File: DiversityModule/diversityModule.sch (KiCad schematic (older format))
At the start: 41 parts, among them IC1 LP38798, IC2 TDA1308A, P1 CONN_02X05, P2 CONN_01X03, Q1 BFP840, U1 sn74lvc1g3157, U2 RX5808

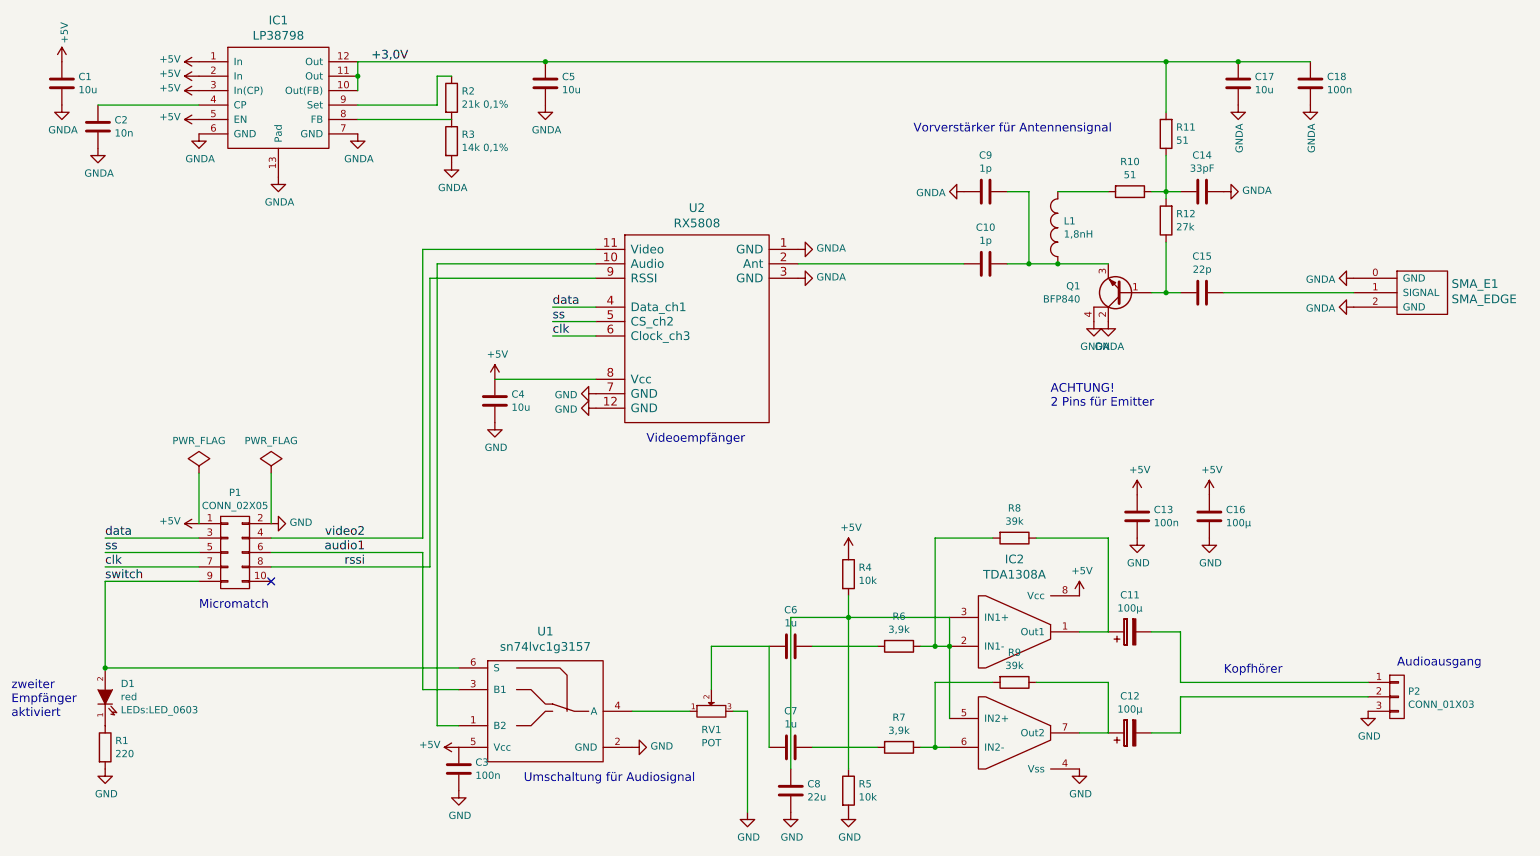
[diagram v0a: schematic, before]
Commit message: Layout fertig. Überprüfung steht aus.
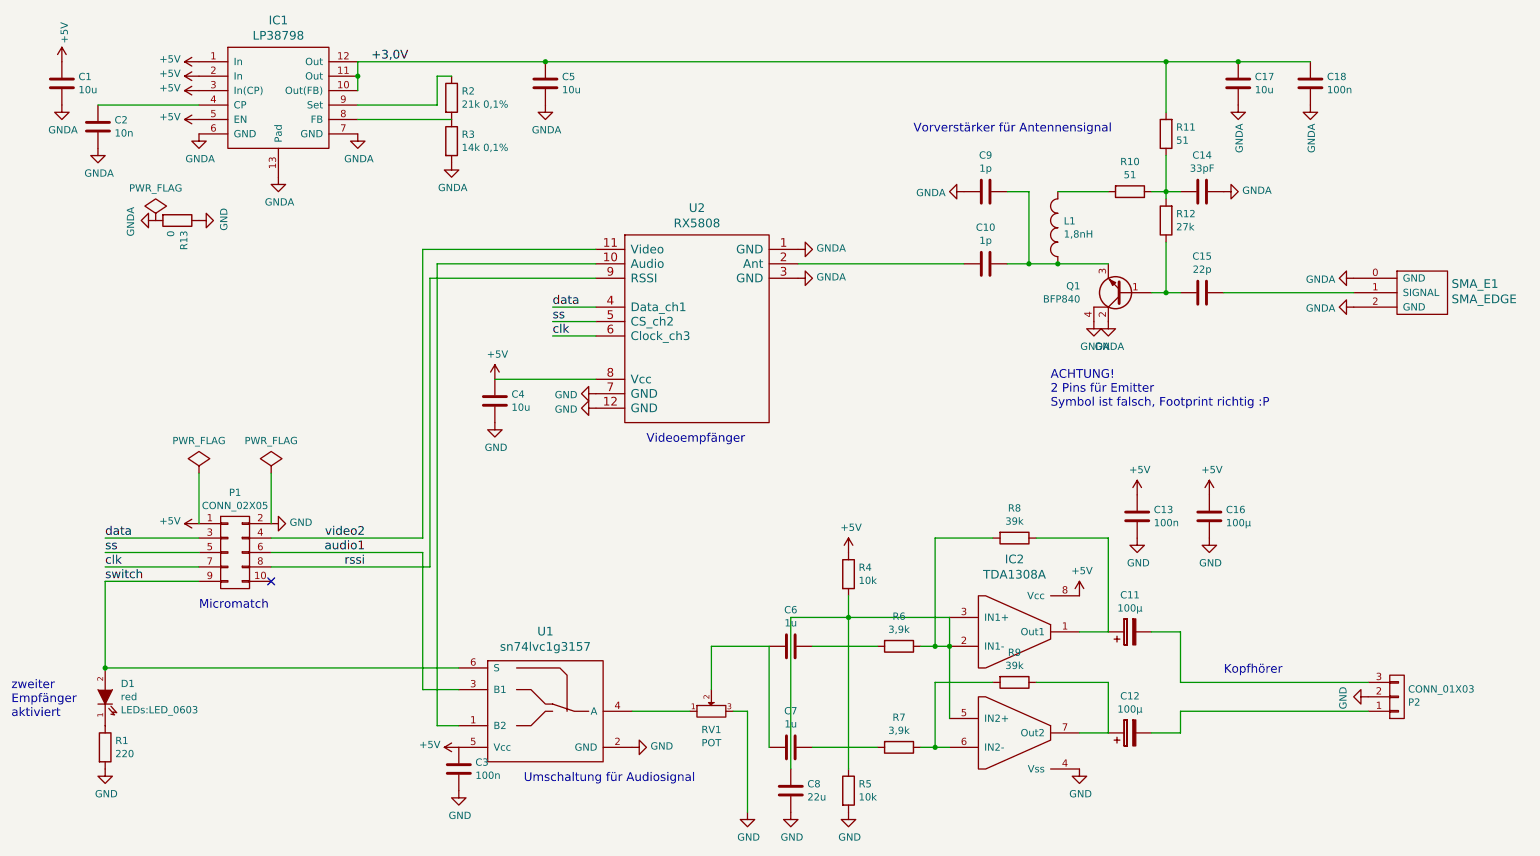
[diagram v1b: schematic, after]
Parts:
- added R13: 0, Resistors_SMD:R_0805, symbol R
- P2: footprint (none) -> PhilippsFootprints:LUM1503-SMD
- RV1: footprint (none) -> PhilippsFootprints:Poti-SMD-Model-23A
- U1: footprint TO_SOT_Packages_SMD:SOT-23-5 -> TO_SOT_Packages_SMD:SOT-23-6
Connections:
- net GND: now also P2.2 (P2), R13.1; no longer P2.3 (P3)
- net GNDA: now also R13.2
- net at P2.1 (P1): now also C12.2; no longer C11.2
- new net: C11.2, P2.3 (P3)
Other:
- note added: "ACHTUNG!\n2 Pins für Emitter\nSymbol ist falsch, Footprint richtig :P"
- note removed: "ACHTUNG!\n2 Pins für Emitter"
- note removed: "Audioausgang"
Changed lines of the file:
@@
 F 0 "U1" H 4400 6053 60  0000 C CNN
 F 1 "sn74lvc1g3157" H 4400 5947 60  0000 C CNN
-F 2 "TO_SOT_Packages_SMD:SOT-23-5" H 3150 5000 60  0001 C CNN
+F 2 "TO_SOT_Packages_SMD:SOT-23-6" H 3150 5000 60  0001 C CNN
 F 3 "" H 3150 5000 60  0000 C CNN
 	1    4400 5500
@@
 F 0 "P2" H 10377 5438 50  0000 L CNN
 F 1 "CONN_01X03" H 10377 5347 50  0000 L CNN
-F 2 "" H 10300 5400 50  0001 C CNN
+F 2 "PhilippsFootprints:LUM1503-SMD" H 10300 5400 50  0001 C CNN
 F 3 "" H 10300 5400 50  0000 C CNN
 	1    10300 5400
-	1    0    0    -1
+	1    0    0    1
 $EndComp
 $Comp
 L GND #PWR013
 U 1 1 5706CAFE
-P 10100 5500
-F 0 "#PWR013" H 10100 5250 50  0001 C CNN
-F 1 "GND" H 10108 5327 50  0000 C CNN
-F 2 "" H 10100 5500 50  0000 C CNN
-F 3 "" H 10100 5500 50  0000 C CNN
-	1    10100 5500
-	1    0    0    -1
+P 10100 5400
+F 0 "#PWR013" H 10100 5150 50  0001 C CNN
+F 1 "GND" H 10108 5227 50  0000 C CNN
+F 2 "" H 10100 5400 50  0000 C CNN
+F 3 "" H 10100 5400 50  0000 C CNN
+	1    10100 5400
+	0    1    1    0
 $EndComp
 Connection ~ 1350 5200
@@
 Text Notes 5100 3650 0    60   ~ 0
 Videoempfänger
-Text Notes 10300 5200 0    60   ~ 0
-Audioausgang
 Text Notes 700  5550 0    60   ~ 0
 zweiter\nEmpfänger\naktiviert
@@
 F 0 "RV1" H 5550 5372 50  0000 C CNN
 F 1 "POT" H 5550 5281 50  0000 C CNN
-F 2 "" H 5550 5500 50  0001 C CNN
+F 2 "PhilippsFootprints:Poti-SMD-Model-23A" H 5550 5500 50  0001 C CNN
 F 3 "" H 5550 5500 50  0000 C CNN
 	1    5550 5500
@@
 Wire Wire Line
 	8600 5650 8800 5650
-Wire Wire Line
-	8800 5650 8800 5400
-Wire Wire Line
-	8800 5400 10100 5400
 Wire Wire Line
 	8600 4950 8800 4950
@@
 $EndComp
 Text Notes 7900 3400 0    60   ~ 0
-ACHTUNG!\n2 Pins für Emitter
+ACHTUNG!\n2 Pins für Emitter\nSymbol ist falsch, Footprint richtig :P
 $Comp
 L GNDA #PWR024
@@
 Connection ~ 8700 1000
 Connection ~ 9200 1000
+Wire Wire Line
+	10100 5500 8800 5500
+Wire Wire Line
+	8800 5500 8800 5650
+$Comp
+L R R13
+U 1 1 570E7730
+P 1850 2100
+F 0 "R13" H 1920 2146 50  0000 L CNN
+F 1 "0" H 1920 2055 50  0000 L CNN
+F 2 "Resistors_SMD:R_0805" V 1780 2100 50  0001 C CNN
+F 3 "" H 1850 2100 50  0000 C CNN
+F 4 "YAG1783CT-ND" H 1850 2100 60  0001 C CNN "Digikeynummer"
+	1    1850 2100
+	0    1    1    0
+$EndComp
+$Comp
+L GNDA #PWR046
+U 1 1 570E786B
+P 1700 2100
+F 0 "#PWR046" H 1700 1850 50  0001 C CNN
+F 1 "GNDA" H 1708 1927 50  0000 C CNN
+F 2 "" H 1700 2100 50  0000 C CNN
+F 3 "" H 1700 2100 50  0000 C CNN
+	1    1700 2100
+	0    1    1    0
+$EndComp
+$Comp
+L GND #PWR047
+U 1 1 570E7948
+P 2000 2100
+F 0 "#PWR047" H 2000 1850 50  0001 C CNN
+F 1 "GND" H 2008 1927 50  0000 C CNN
+F 2 "" H 2000 2100 50  0000 C CNN
+F 3 "" H 2000 2100 50  0000 C CNN
+	1    2000 2100
+	0    -1   -1   0
+$EndComp
+$Comp
+L PWR_FLAG #FLG048
+U 1 1 570E7D78
+P 1700 2100
+F 0 "#FLG048" H 1700 2195 50  0001 C CNN
+F 1 "PWR_FLAG" H 1700 2324 50  0000 C CNN
+F 2 "" H 1700 2100 50  0000 C CNN
+F 3 "" H 1700 2100 50  0000 C CNN
+	1    1700 2100
+	1    0    0    -1
+$EndComp
 $EndSCHEMATC

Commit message: BOM für beide platinen des kompletten moduls dazugefügt
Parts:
- SMA_E1: footprint PhilippsFootprints:SMA_EDGE_small -> PhilippsFootprints:SMA_EDGE_Johnson_142-0701-801
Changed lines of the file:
@@
 F 0 "SMA_E1" H 10678 2661 60  0000 L CNN
 F 1 "SMA_EDGE" H 10678 2555 60  0000 L CNN
-F 2 "PhilippsFootprints:SMA_EDGE_small" H 10350 2600 60  0001 C CNN
+F 2 "PhilippsFootprints:SMA_EDGE_Johnson_142-0701-801" H 10350 2600 60  0001 C CNN
 F 3 "" H 10350 2600 60  0000 C CNN
 	1    10350 2600

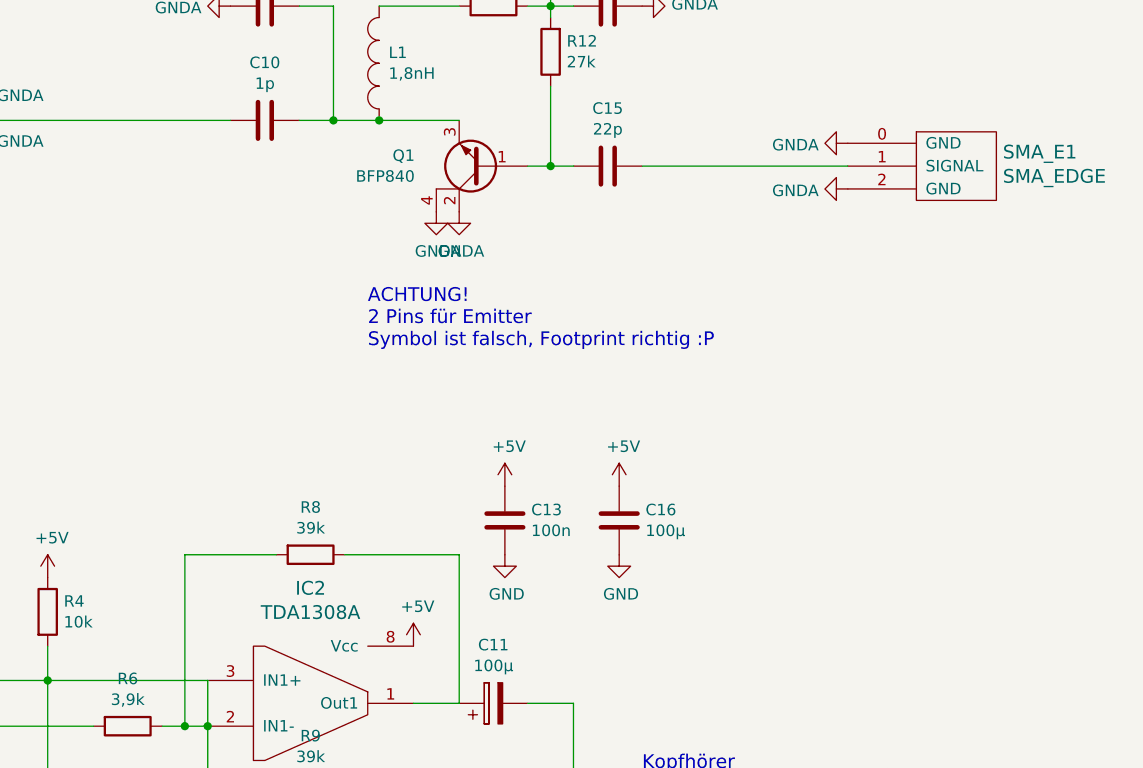
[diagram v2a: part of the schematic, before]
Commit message: Layoutänderungen für videoumschalter (anderes gehäuse)
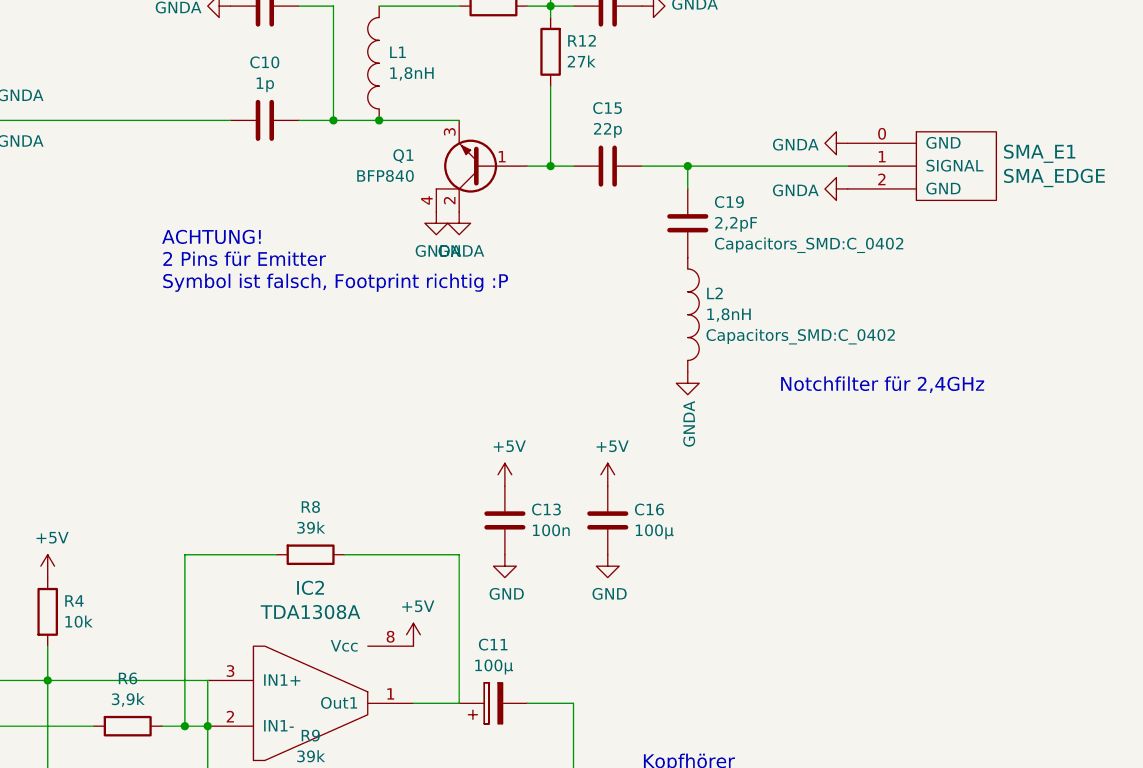
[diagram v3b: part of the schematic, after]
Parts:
- added C19: 2,2pF, Capacitors_SMD:C_0402, symbol C
- added L2: 1,8nH, Capacitors_SMD:C_0402, symbol INDUCTOR_SMALL
- U1: footprint TO_SOT_Packages_SMD:SOT-23-6 -> TO_SOT_Packages_SMD:SC-70-6
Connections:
- net GNDA: now also L2.2
- net at C15.1, SMA_E1.1 (SIGNAL): now also C19.1
- new net: C19.2, L2.1
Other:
- note added: "Notchfilter für 2,4GHz"
- moved on the sheet: C16
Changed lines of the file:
@@
 Title "Diversity-Zusatzmodul"
 Date "2016-04-07"
-Rev "0.1"
+Rev "0.2"
 Comp ""
 Comment1 ""
@@
 F 0 "U1" H 4400 6053 60  0000 C CNN
 F 1 "sn74lvc1g3157" H 4400 5947 60  0000 C CNN
-F 2 "TO_SOT_Packages_SMD:SOT-23-6" H 3150 5000 60  0001 C CNN
+F 2 "TO_SOT_Packages_SMD:SC-70-6" H 3150 5000 60  0001 C CNN
 F 3 "" H 3150 5000 60  0000 C CNN
 	1    4400 5500
@@
 L C C16
 U 1 1 5706F496
-P 9000 4150
-F 0 "C16" H 9115 4196 50  0000 L CNN
-F 1 "100µ" H 9115 4105 50  0000 L CNN
-F 2 "Capacitors_SMD:C_1210" H 9038 4000 50  0001 C CNN
-F 3 "" H 9000 4150 50  0000 C CNN
-	1    9000 4150
+P 8950 4150
+F 0 "C16" H 9065 4196 50  0000 L CNN
+F 1 "100µ" H 9065 4105 50  0000 L CNN
+F 2 "Capacitors_SMD:C_1210" H 8988 4000 50  0001 C CNN
+F 3 "" H 8950 4150 50  0000 C CNN
+	1    8950 4150
 	1    0    0    -1
 $EndComp
@@
 L GND #PWR021
 U 1 1 5706F561
-P 9000 4300
-F 0 "#PWR021" H 9000 4050 50  0001 C CNN
-F 1 "GND" H 9008 4127 50  0000 C CNN
-F 2 "" H 9000 4300 50  0000 C CNN
-F 3 "" H 9000 4300 50  0000 C CNN
-	1    9000 4300
+P 8950 4300
+F 0 "#PWR021" H 8950 4050 50  0001 C CNN
+F 1 "GND" H 8958 4127 50  0000 C CNN
+F 2 "" H 8950 4300 50  0000 C CNN
+F 3 "" H 8950 4300 50  0000 C CNN
+	1    8950 4300
 	1    0    0    -1
 $EndComp
@@
 L +5V #PWR023
 U 1 1 5706F6CB
-P 9000 4000
-F 0 "#PWR023" H 9000 3850 50  0001 C CNN
-F 1 "+5V" H 9018 4173 50  0000 C CNN
-F 2 "" H 9000 4000 50  0000 C CNN
-F 3 "" H 9000 4000 50  0000 C CNN
-	1    9000 4000
+P 8950 4000
+F 0 "#PWR023" H 8950 3850 50  0001 C CNN
+F 1 "+5V" H 8968 4173 50  0000 C CNN
+F 2 "" H 8950 4000 50  0000 C CNN
+F 3 "" H 8950 4000 50  0000 C CNN
+	1    8950 4000
 	1    0    0    -1
 $EndComp
@@
 	-1   0    0    1
 $EndComp
-Text Notes 7900 3400 0    60   ~ 0
+Text Notes 7000 3150 0    60   ~ 0
 ACHTUNG!\n2 Pins für Emitter\nSymbol ist falsch, Footprint richtig :P
 $Comp
@@
 	8700 2250 8700 2600
 Connection ~ 8700 2600
-Wire Wire Line
-	9100 2600 10000 2600
 $Comp
 L LP38798 IC1
@@
 	1    0    0    -1
 $EndComp
+$Comp
+L INDUCTOR_SMALL L2
+U 1 1 5756C8B7
+P 9300 3250
+F 0 "L2" V 9209 3328 50  0000 L CNN
+F 1 "1,8nH" V 9300 3328 50  0000 L CNN
+F 2 "Capacitors_SMD:C_0402" V 9391 3328 50  0000 L CNN
+F 3 "" H 9300 3250 50  0000 C CNN
+	1    9300 3250
+	0    1    1    0
+$EndComp
+$Comp
+L C C19
+U 1 1 5756CADB
+P 9300 2850
+F 0 "C19" H 9415 2941 50  0000 L CNN
+F 1 "2,2pF" H 9415 2850 50  0000 L CNN
+F 2 "Capacitors_SMD:C_0402" H 9415 2759 50  0000 L CNN
+F 3 "" H 9300 2850 50  0000 C CNN
+	1    9300 2850
+	1    0    0    -1
+$EndComp
+$Comp
+L GNDA #PWR049
+U 1 1 5756CC4F
+P 9300 3500
+F 0 "#PWR049" H 9300 3250 50  0001 C CNN
+F 1 "GNDA" V 9308 3373 50  0000 R CNN
+F 2 "" H 9300 3500 50  0000 C CNN
+F 3 "" H 9300 3500 50  0000 C CNN
+	1    9300 3500
+	1    0    0    -1
+$EndComp
+Wire Wire Line
+	10000 2600 9100 2600
+Wire Wire Line
+	9300 2700 9300 2600
+Connection ~ 9300 2600
+Text Notes 9700 3600 0    60   ~ 0
+Notchfilter für 2,4GHz
 $EndSCHEMATC

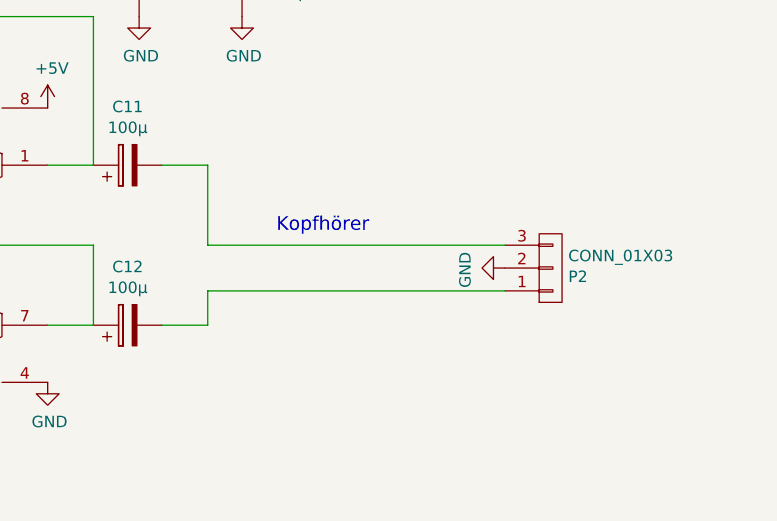
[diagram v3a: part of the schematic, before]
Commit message: Klinkenbuchse ausgetauscht und zur Lib hinzugefügt.
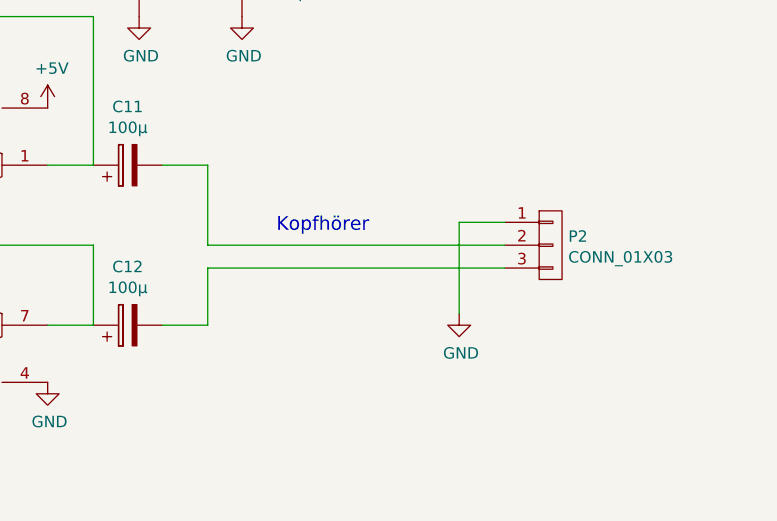
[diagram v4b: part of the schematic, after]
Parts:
- P2: footprint PhilippsFootprints:LUM1503-SMD -> PhilippsFootprints:LUM1503-03
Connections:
- net GND: now also P2.1 (P1); no longer P2.2 (P2)
- net at C12.2: now also P2.3 (P3); no longer P2.1 (P1)
- net at C11.2: now also P2.2 (P2); no longer P2.3 (P3)
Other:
- moved on the sheet: P2
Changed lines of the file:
@@
 L CONN_01X03 P2
 U 1 1 5706C9D5
-P 10300 5400
-F 0 "P2" H 10377 5438 50  0000 L CNN
-F 1 "CONN_01X03" H 10377 5347 50  0000 L CNN
-F 2 "PhilippsFootprints:LUM1503-SMD" H 10300 5400 50  0001 C CNN
-F 3 "" H 10300 5400 50  0000 C CNN
-	1    10300 5400
-	1    0    0    1
+P 10300 5300
+F 0 "P2" H 10377 5338 50  0000 L CNN
+F 1 "CONN_01X03" H 10377 5247 50  0000 L CNN
+F 2 "PhilippsFootprints:LUM1503-03" H 10300 5300 50  0001 C CNN
+F 3 "" H 10300 5300 50  0000 C CNN
+	1    10300 5300
+	1    0    0    -1
 $EndComp
 $Comp
 L GND #PWR013
 U 1 1 5706CAFE
-P 10100 5400
-F 0 "#PWR013" H 10100 5150 50  0001 C CNN
-F 1 "GND" H 10108 5227 50  0000 C CNN
-F 2 "" H 10100 5400 50  0000 C CNN
-F 3 "" H 10100 5400 50  0000 C CNN
-	1    10100 5400
-	0    1    1    0
+P 9900 5600
+F 0 "#PWR013" H 9900 5350 50  0001 C CNN
+F 1 "GND" H 9908 5427 50  0000 C CNN
+F 2 "" H 9900 5600 50  0000 C CNN
+F 3 "" H 9900 5600 50  0000 C CNN
+	1    9900 5600
+	1    0    0    -1
 $EndComp
 Connection ~ 1350 5200
@@
 $EndComp
 Wire Wire Line
-	8600 5650 8800 5650
+	8800 5650 8600 5650
 Wire Wire Line
 	8600 4950 8800 4950
@@
 Connection ~ 9200 1000
 Wire Wire Line
-	10100 5500 8800 5500
-Wire Wire Line
-	8800 5500 8800 5650
+	8800 5400 8800 5650
 $Comp
 L R R13
@@
 Text Notes 9700 3600 0    60   ~ 0
 Notchfilter für 2,4GHz
+Wire Wire Line
+	10100 5400 8800 5400
+Wire Wire Line
+	9900 5600 9900 5200
+Wire Wire Line
+	9900 5200 10100 5200
 $EndSCHEMATC

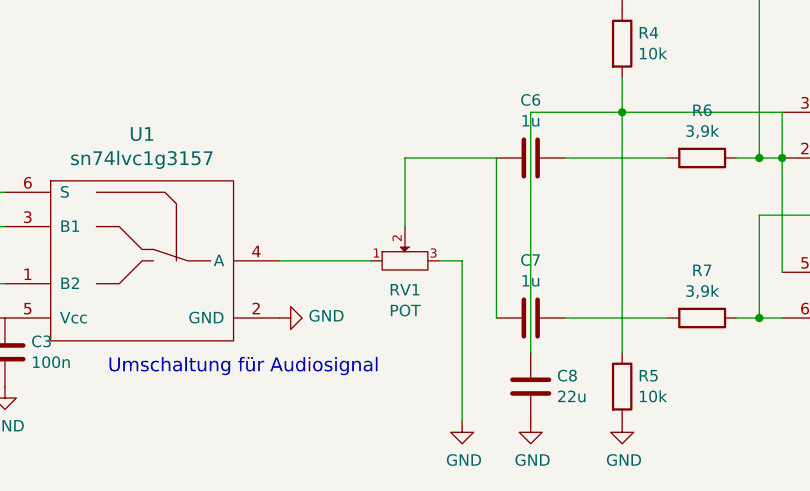
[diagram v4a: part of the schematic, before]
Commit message: BOM hinzugefügt
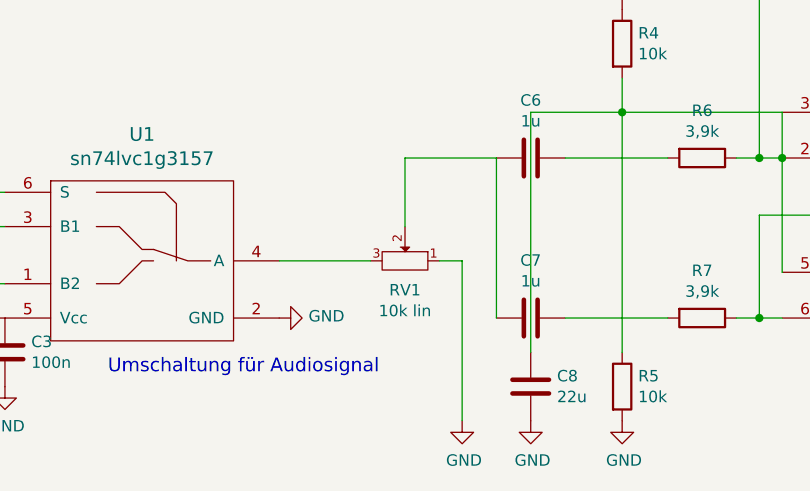
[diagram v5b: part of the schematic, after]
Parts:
- RV1: value POT -> 10k lin; Reichelt-Nummer (none) -> 23A-10K
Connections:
- net GND: now also RV1.1; no longer RV1.3
- net at U1.4 (A): now also RV1.3; no longer RV1.1
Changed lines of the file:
@@
 P 5550 5500
 F 0 "RV1" H 5550 5372 50  0000 C CNN
-F 1 "POT" H 5550 5281 50  0000 C CNN
+F 1 "10k lin" H 5550 5281 50  0000 C CNN
 F 2 "PhilippsFootprints:Poti-SMD-Model-23A" H 5550 5500 50  0001 C CNN
 F 3 "" H 5550 5500 50  0000 C CNN
+F 4 "23A-10K" H 5550 5500 60  0001 C CNN "Reichelt-Nummer"
 	1    5550 5500
-	1    0    0    -1
+	-1   0    0    -1
 $EndComp
 Wire Wire Line
